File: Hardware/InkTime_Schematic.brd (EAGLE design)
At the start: 46 x 35 mm, 105 parts, among them IC1 BQ25180YBGR, IC2 DRV2605YZFR, IC3 BMA423, IC9 RT6160AWSC, J1 503480-2400, J2 TC2030-IDC, J4 KH-TYPE-C-16P, Q1 20V/4.2A/52mΩ/1.4W, Q3 SI1308EDL-T1-GE3, U1 NRF52840_QF, U3 MAX17048G+T10, X1 32MHz, X2 32.768kHz

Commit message: Added files + README
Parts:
- moved R9 0.93 mm to (127.0, 19.7), turned to 90 degrees
- moved R5 0.62 mm to (112.6, 13.6), turned to 90 degrees
- moved C15 0.56 mm to (130.2, 34.3)
- moved L2 0.56 mm to (128.0, 34.0)
- moved L3 0.56 mm to (129.0, 33.9)
- moved TP_3V3 0.35 mm to (119.5, 20.9)
- moved C21 0.32 mm to (124.2, 23.1)
- moved TP_ON 0.28 mm to (123.9, 16.3)
- moved TP4 0.12 mm to (129.5, 24.0)
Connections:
- removed net 3V3/1.7D: C34.2, IC2.C2, Q1.2, R5.2, R7.2, R8.2, R_PWR_EPD.2
- removed net 3V3/2.4A: C12.1, C14.1, C19.1, C25.1, C33.1, C6.1, C7.1, C8.1, IC3.10, IC3.3, IC3.7, IC9.E2, IC9.E3, J2.1, R17.1, R18.1, TP5.TP, TP_3V3.TP, U1.P$A22, U1.P$AD14, U1.P$AD23, U1.P$B1, U1.P$W1, U1.P$Y2
- removed net ALERT/1.6C: U3.5
- removed net ALERT/2.5C: U1.P$J24
- removed net D+/1.5D: D3.4
- removed net D+/2.7D: U1.P$AD6
- removed net D-/1.5D: D3.6
- removed net D-/2.7D: U1.P$AD4
- removed net EPD_BUSY/1.5D: J1.9
- removed net EPD_BUSY/2.2D: U1.P$AD12
- removed net EPD_CS/1.4C: J1.12
- removed net EPD_CS/2.2D: U1.P$K2
- removed net EPD_DC/1.5D: J1.11
- removed net EPD_DC/2.2D: U1.P$AD10
- removed net EPD_RST/1.5D: J1.10
- removed net EPD_RST/2.2D: U1.P$AC11
- removed net HAPTIC_EN/1.4A: IC2.A1
- removed net HAPTIC_EN/2.6A: U1.P$U1
- removed net MOSI/1.5B: J1.14
- removed net MOSI/2.2D: U1.P$B13
- removed net P0.13/1.5D: C30.1, R5.1, SW_UP.2
- removed net P0.13/2.6C: U1.P$AD8
- removed net P0.14/1.5D: C31.1, R8.1, SW_ENT.2
- removed net P0.14/2.7C: U1.P$AC9
- removed net P1.01/1.6C: Q1.1, R_PWR_EPD.1
- removed net P1.01/2.4B: U1.P$Y23
- removed net P1.02/1.6C: C29.1, R7.1, SW_DN.2
- removed net P1.02/2.8C: U1.P$W24
- removed net SCK/1.5B: J1.13
- removed net SCK/2.2D: U1.P$A12
- removed net SCL/1.4C: IC2.C1, U3.7
- removed net SCL/2.4C: IC1.B1, IC3.12, R17.2, R4.1, TP_SCL.TP, U1.P$M2
- removed net SDA/1.4C: IC2.B2, U3.8
- removed net SDA/2.4C: IC1.C1, IC3.2, R18.2, R2.1, TP_SDA.TP, U1.P$L1
- removed net VBAT/1.2A: C27.1, TP_VBAT.TP, U3.2, U3.3
- removed net VBAT/2.5C: C37.2, IC1.C2
- removed net VBUS/1.5D: C42.1, C43.1, D3.5, J4.A4_B9, J4.A9_B4
- removed net VBUS/2.6D: C21.1, C38.2, IC1.A2, U1.P$AD2
- new net 3V3: C12.1, C14.1, C19.1, C25.1, C33.1, C34.2, C6.1, C7.1, C8.1, IC2.C2, IC3.10, IC3.3, IC3.7, IC9.E2, IC9.E3, J2.1, Q1.2, R17.1, R18.1, R5.2, R7.2, R8.2, R_PWR_EPD.2, TP5.TP, TP_3V3.TP, U1.P$A22, U1.P$AD14, U1.P$AD23, U1.P$B1, U1.P$W1, U1.P$Y2
- new net ALERT: U1.P$J24, U3.5
- new net D+: D3.4, U1.P$AD6
- new net D-: D3.6, U1.P$AD4
- new net EPD_BUSY: J1.9, U1.P$AD12
- new net EPD_CS: J1.12, U1.P$K2
- new net EPD_DC: J1.11, U1.P$AD10
- new net EPD_RST: J1.10, U1.P$AC11
- new net HAPTIC_EN: IC2.A1, U1.P$U1
- new net MOSI: J1.14, U1.P$B13
- new net P0.13: C30.1, R5.1, SW_UP.2, U1.P$AD8
- new net P0.14: C31.1, R8.1, SW_ENT.2, U1.P$AC9
- new net P1.01: Q1.1, R_PWR_EPD.1, U1.P$Y23
- new net P1.02: C29.1, R7.1, SW_DN.2, U1.P$W24
- new net SCK: J1.13, U1.P$A12
- new net SCL: IC1.B1, IC2.C1, IC3.12, R17.2, R4.1, TP_SCL.TP, U1.P$M2, U3.7
- new net SDA: IC1.C1, IC2.B2, IC3.2, R18.2, R2.1, TP_SDA.TP, U1.P$L1, U3.8
- new net VBAT: C27.1, C37.2, IC1.C2, TP_VBAT.TP, U3.2, U3.3
- new net VBUS: C21.1, C38.2, C42.1, C43.1, D3.5, IC1.A2, J4.A4_B9, J4.A9_B4, U1.P$AD2
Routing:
- net 3V3: track 0.00 -> 154.8 mm, vias 0 -> 14
- net 3V3/2.4A: track 102.7 -> 0.00 mm, vias 10 -> 0
- net SCL: track 0.00 -> 68.2 mm, vias 0 -> 7
- net P1.01: track 0.00 -> 60.4 mm, vias 0 -> 2
- net P0.13: track 0.00 -> 56.6 mm, vias 0 -> 2
- net SDA: track 0.00 -> 51.5 mm, vias 0 -> 10
- net EPD_DC: track 0.00 -> 48.0 mm, vias 0 -> 2
- net EPD_RST: track 0.00 -> 46.2 mm, vias 0 -> 2
- net 3V3/1.7D: track 43.9 -> 0.00 mm, vias 4 -> 0
- net SCL/2.4C: track 42.2 -> 0.00 mm, vias 4 -> 0
- net VBUS: track 0.00 -> 42.0 mm, vias 0 -> 2
- net EPD_BUSY: track 0.00 -> 41.5 mm, vias 0 -> 2
- net D+: track 0.00 -> 36.9 mm, vias 0 -> 2
- net MOSI: track 0.00 -> 36.7 mm, vias 0 -> 2
- net ALERT: track 0.00 -> 35.2 mm, vias 0 -> 2
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
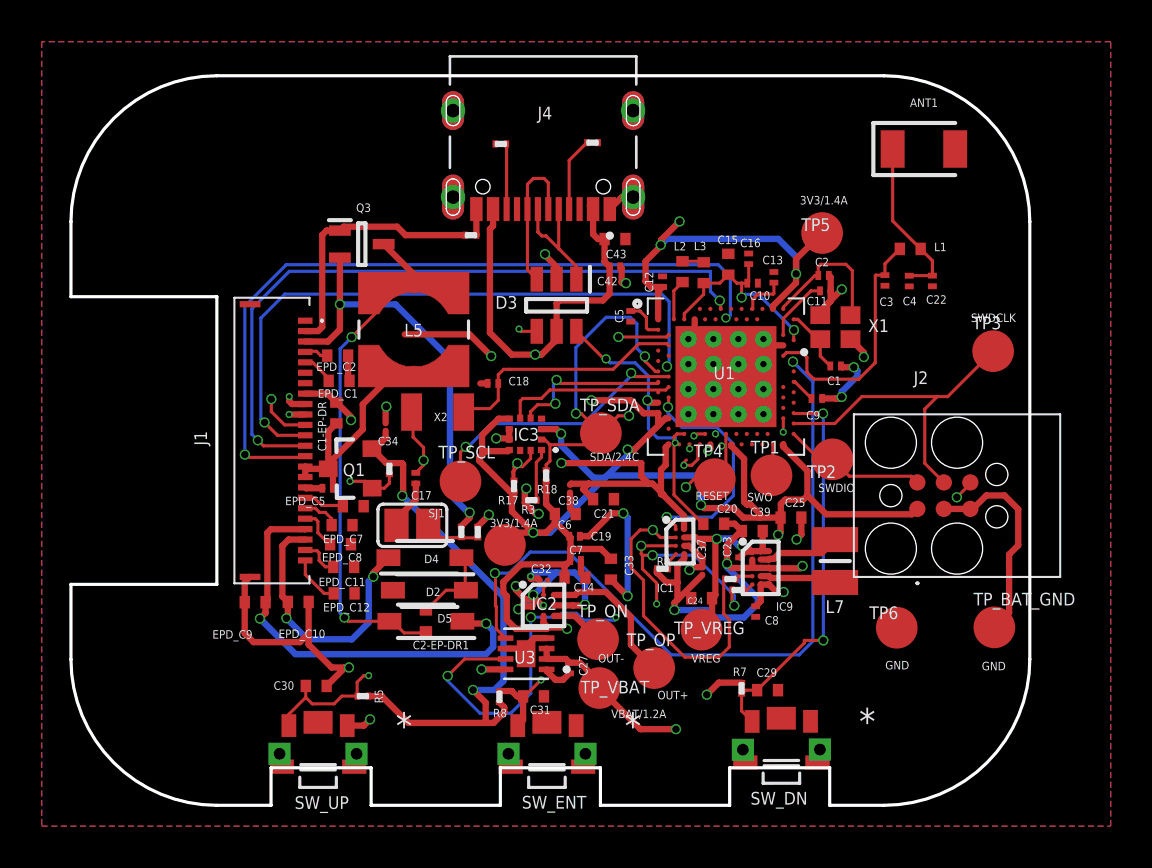
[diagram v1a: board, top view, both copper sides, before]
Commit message: Fixed routing errors
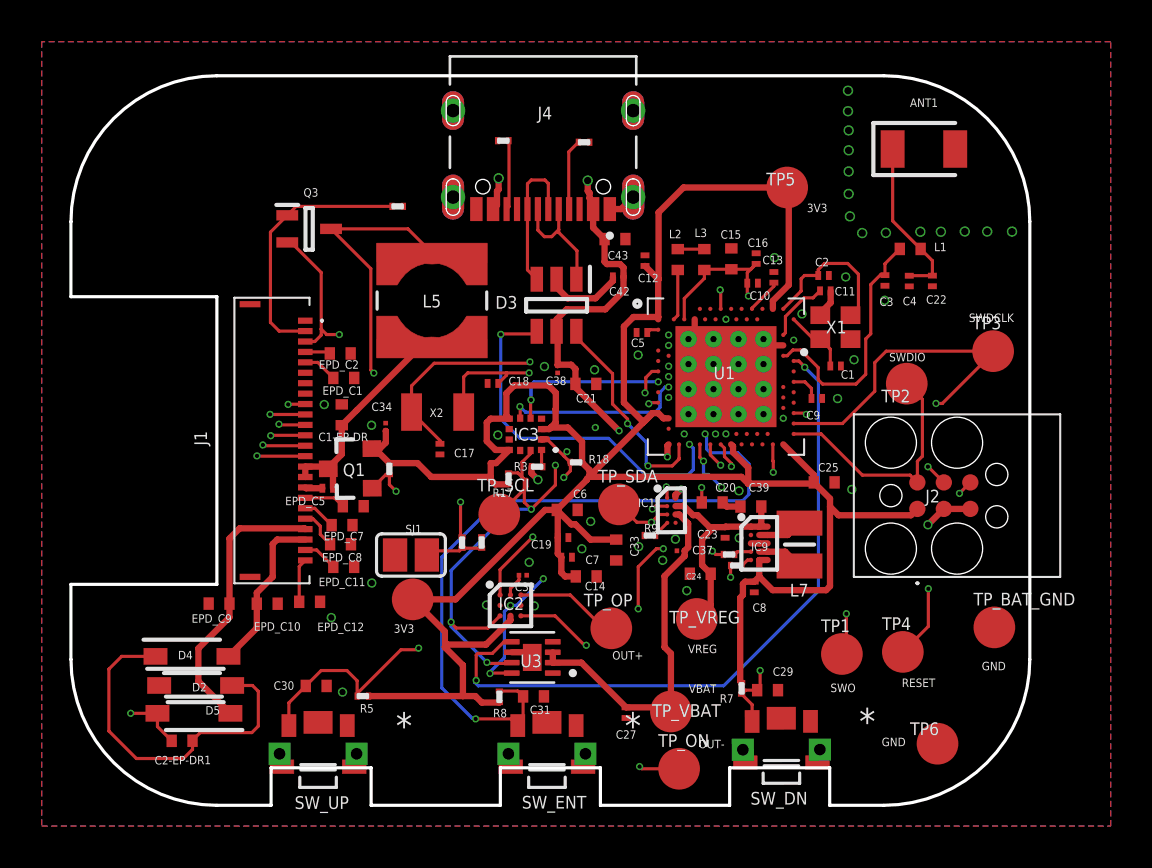
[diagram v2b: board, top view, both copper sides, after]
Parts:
- moved C2-EP-DR1 13.0 mm to (104.0, 11.5), turned to 180.3 degrees
- moved TP4 12.2 mm to (138.5, 15.7)
- moved D4 12.1 mm to (104.4, 15.5), turned to 0 degrees
- moved D2 12.1 mm to (104.6, 14.1)
- moved D5 12.0 mm to (104.5, 12.8)
- moved TP1 9.21 mm to (135.6, 15.6)
- moved TP_ON 7.33 mm to (127.8, 10.1)
- moved TP6 5.90 mm to (140.2, 11.3)
- moved C38 5.77 mm to (122.0, 29.3)
- moved C21 5.60 mm to (123.3, 28.6)
- moved TP_3V3 5.14 mm to (115.0, 18.3)
- moved TP2 5.09 mm to (138.7, 28.6)
- moved R2_EP_DR 3.78 mm to (114.3, 37.1)
- moved TP_VBAT 3.62 mm to (127.4, 12.9)
- moved TP_SDA 3.52 mm to (124.9, 22.8)
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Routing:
- net GND: track 139.2 -> 16.3 mm, vias 24 -> 43
- net 3V3: track 154.8 -> 125.3 mm, vias 14 -> 0
- net P1.01: track 60.4 -> 31.0 mm
- net SCL: track 68.2 -> 44.2 mm
- net P0.13: track 56.6 -> 34.5 mm, vias 2 -> 5
- net EPD_DC: track 48.0 -> 27.0 mm
- net D+: track 36.9 -> 17.6 mm
- net EPD_RST: track 46.2 -> 27.0 mm
- net EPD_BUSY: track 41.5 -> 25.8 mm
- net N$7: track 24.5 -> 39.2 mm
- net SDA: track 51.5 -> 37.2 mm, vias 10 -> 8
- net N$25: track 3.96 -> 17.1 mm
- net VBUS: track 42.0 -> 29.5 mm, vias 2 -> 5
- net SWO: track 1.51 -> 11.6 mm, vias 0 -> 2
- net OUT-: track 2.58 -> 12.6 mm, vias 0 -> 2
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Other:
- board text added: "3V3"
- board text added: "VBAT"
- board text removed: "3V3/1.4A"
- board text removed: "SDA/2.4C"
- board text removed: "VBAT/1.2A"
